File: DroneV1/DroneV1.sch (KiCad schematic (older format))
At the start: 1 part

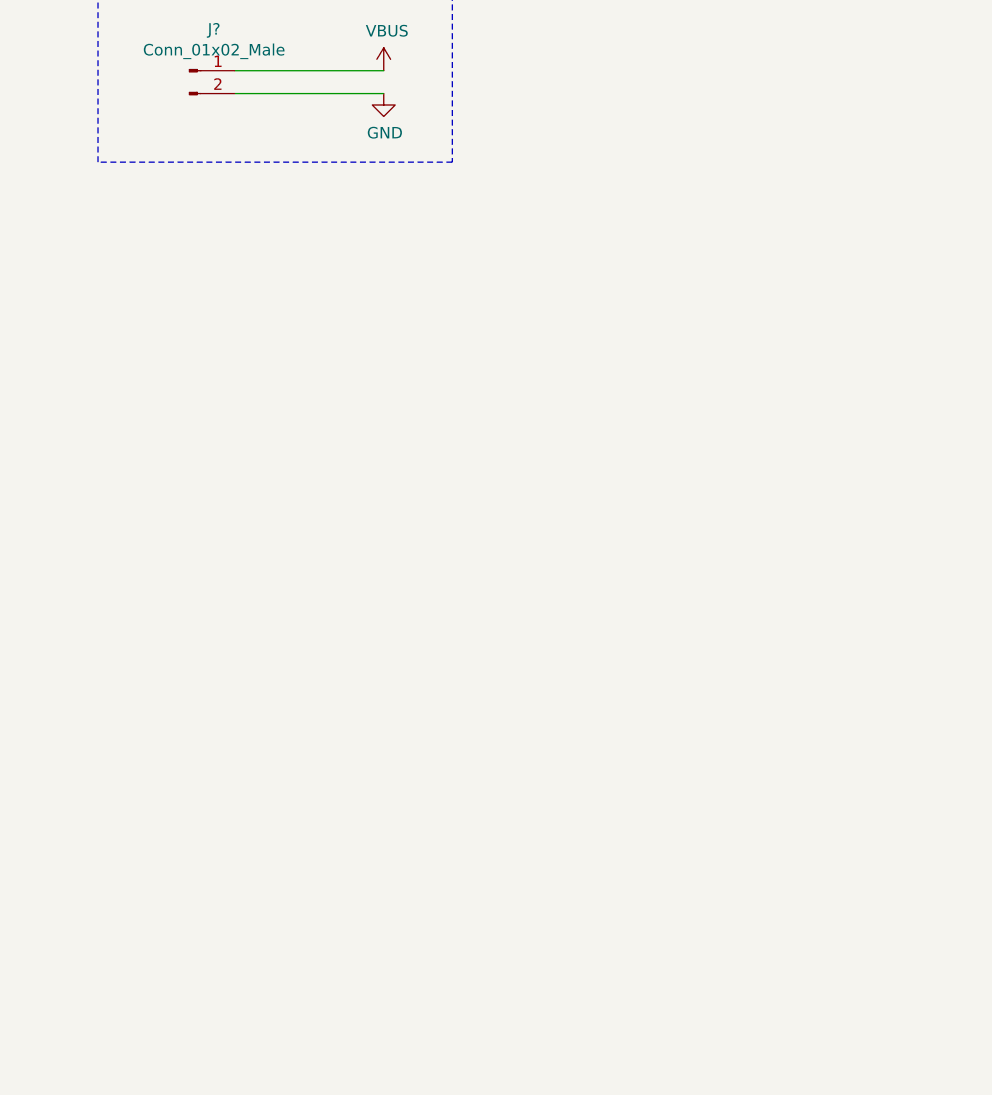
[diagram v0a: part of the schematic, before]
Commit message: Added sensors, power regulation
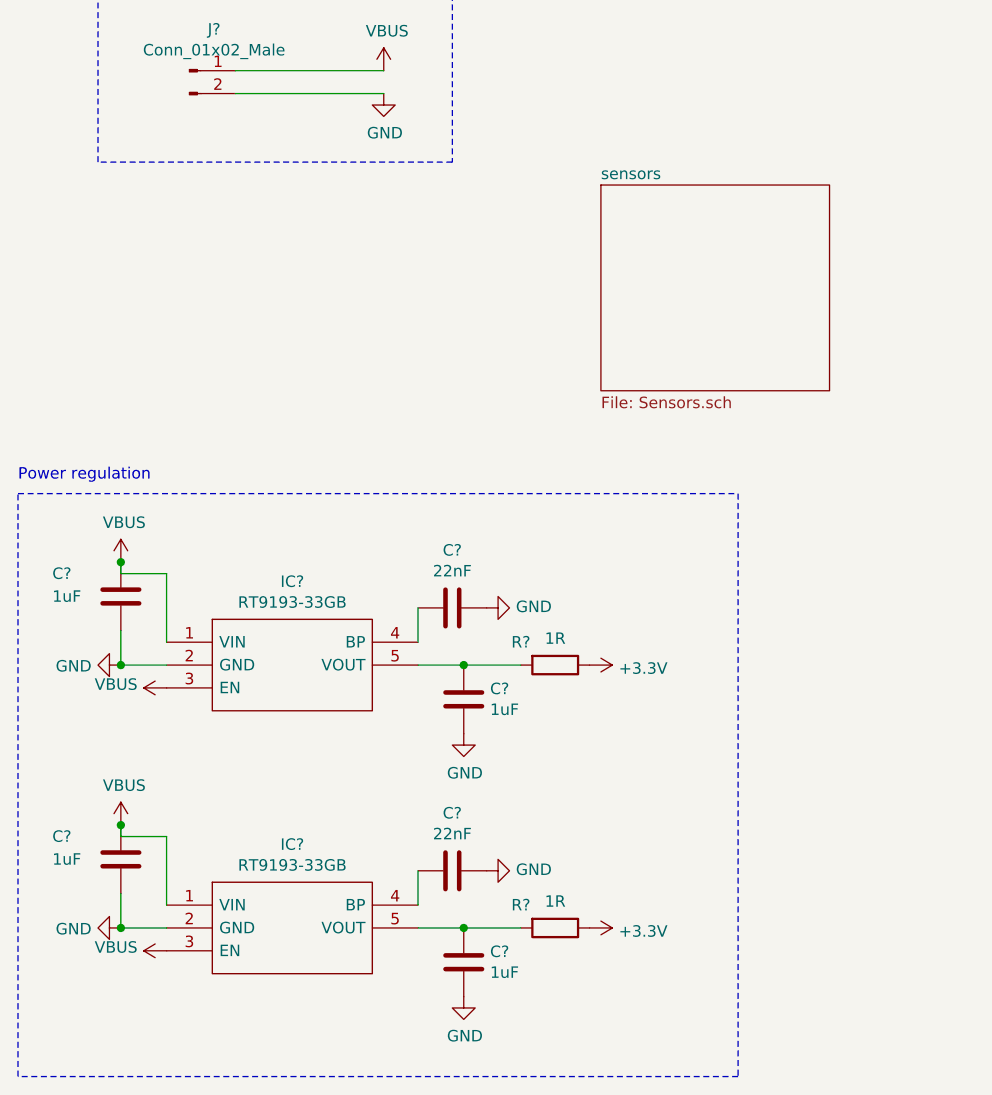
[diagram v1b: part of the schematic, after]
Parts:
- added C? (x4): 1uF, symbol Device:C
- added C? (x2): 22nF, symbol Device:C
- added IC? (x2): RT9193-33GB, SOT94P279X130-5N, symbol RT9193-33GB:RT9193-33GB
- added R? (x2): 1R, symbol Device:R
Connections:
- net GND: now also C?.1, C?.1, C?.2, C?.2, C?.2, C?.2, IC?.2 (GND), IC?.2 (GND)
- net VBUS: now also C?.1, C?.1, IC?.1 (VIN), IC?.1 (VIN), IC?.3 (EN), IC?.3 (EN)
- new net: C?.2, IC?.4 (BP) (x2)
- new net: C?.1, IC?.5 (VOUT), R?.2 (x2)
- new net +3V3: R?.1, R?.1
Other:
- note added: "Power regulation"

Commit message: Added indicator LEDs
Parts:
- added D1, D2, D3, D4: LED, LED_SMD:LED_0201_0603Metric, symbol Device:LED
- added Q5, Q6, Q7, Q8: AO3402, SOT95P280X125-3N, symbol AO3402:AO3402
- added R11, R15, R17: 10k, Resistor_SMD:R_0603_1608Metric, symbol Device:R
- added R12, R14: 75R, Resistor_SMD:R_0402_1005Metric, symbol Device:R
- added R13: 10k, Resistor_SMD:R_0201_0603Metric, symbol Device:R
- added R16, R18: 47R, Resistor_SMD:R_0603_1608Metric, symbol Device:R
- added U5: DroneOutline, DroneV1:DroneOutlineOLD, symbol DroneSymbol:DroneOutline
- C4, C5, C6, C7, C8, C9: renamed from C?; footprint (none) -> Capacitor_SMD:C_0603_1608Metric
- IC2, IC3: renamed from IC?; footprint SOT94P279X130-5N -> RT9193-33GB:SOT94P279X130-5N
- J1: renamed from J?; footprint (none) -> Connector_JST:JST_PH_S2B-PH-K_1x02_P2.00mm_Horizontal
- R10, R9: renamed from R?; footprint (none) -> Resistor_SMD:R_0603_1608Metric
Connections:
- net GND: now also Q5.2, Q6.2, Q7.2, Q8.2, R11.2, R13.2, R15.2, R17.2
- net VBUS: now also R12.2, R14.2, R16.1, R18.1
- new net: D1.1 (K), Q5.3
- new net: D1.2 (A), R12.1
- new net: D2.1 (K), Q6.3
- new net: D2.2 (A), R14.1
- new net: D3.1 (K), Q7.3
- new net: D3.2 (A), R16.2
- new net: D4.1 (K), Q8.3
- new net: D4.2 (A), R18.2
- new net ledGreen: Q7.1, Q8.1, R15.1, R17.1
- new net ledRed: Q5.1, Q6.1, R11.1, R13.1
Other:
- note added: "Position LED's Starbord/Port\n"
